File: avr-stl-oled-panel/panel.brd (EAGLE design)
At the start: 68 x 42.8 mm, 13 parts

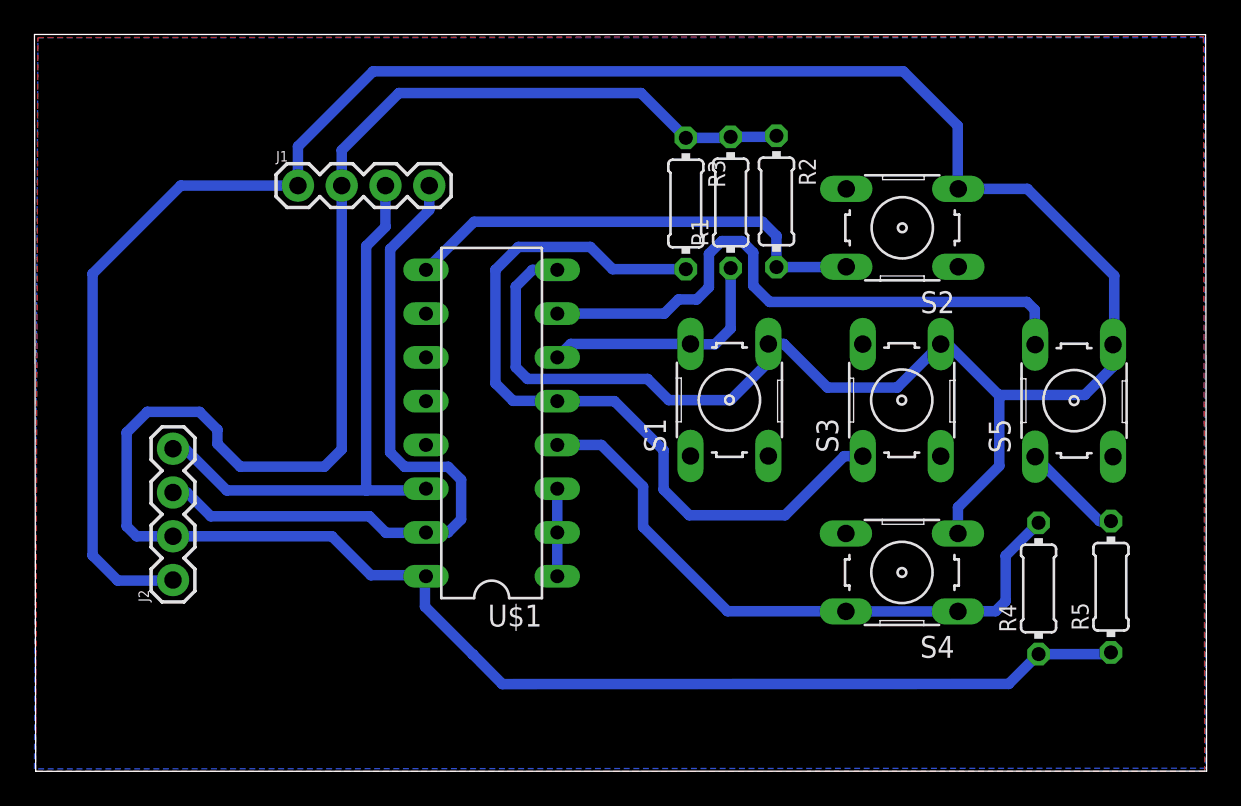
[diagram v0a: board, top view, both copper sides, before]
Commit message: adjusting oled position
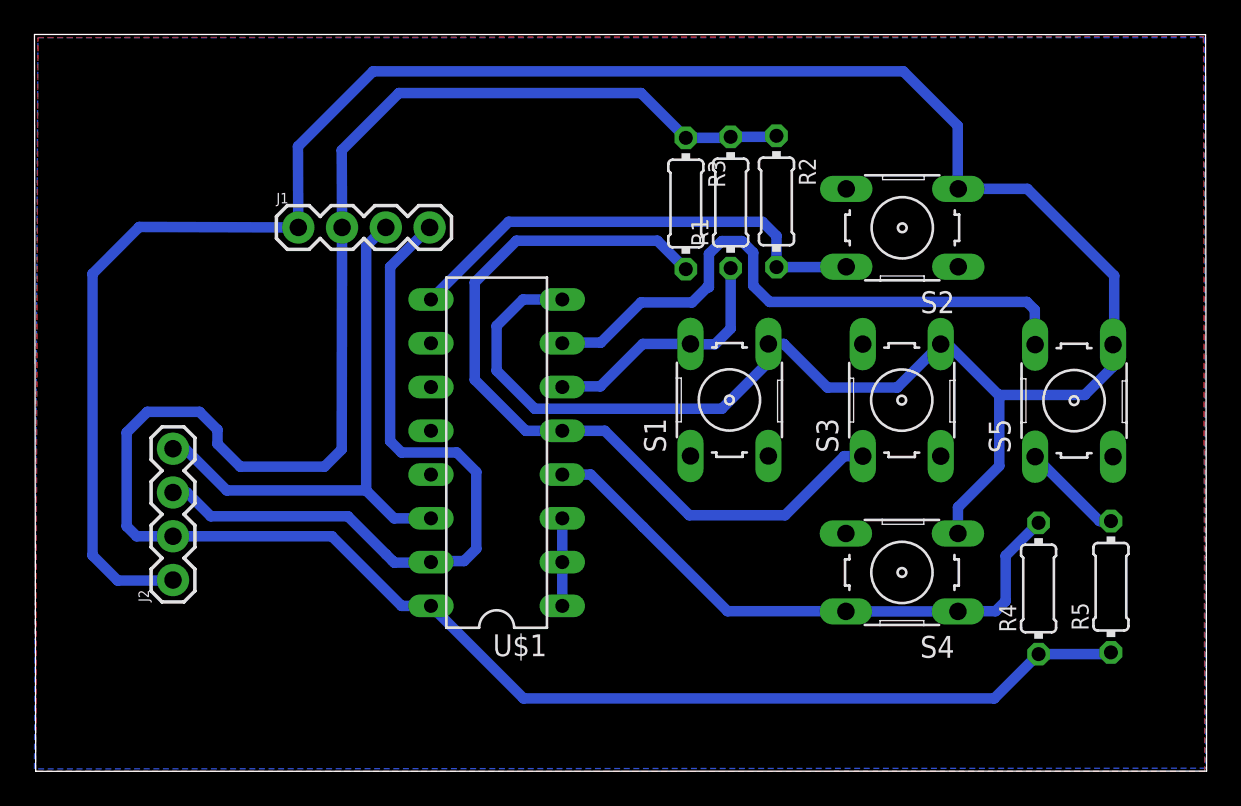
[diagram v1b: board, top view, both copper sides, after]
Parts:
- moved J1 2.43 mm to (15.3, 39.6)
- moved U$1 1.74 mm to (26.8, 26.5)
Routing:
- net GND: track 162.5 -> 164.9 mm
- net B3: track 37.0 -> 34.6 mm
- net N$4: track 41.5 -> 43.2 mm
- net N$5: track 33.9 -> 32.5 mm
- net B2: track 46.0 -> 46.8 mm

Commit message: changing oled panel chip to smd
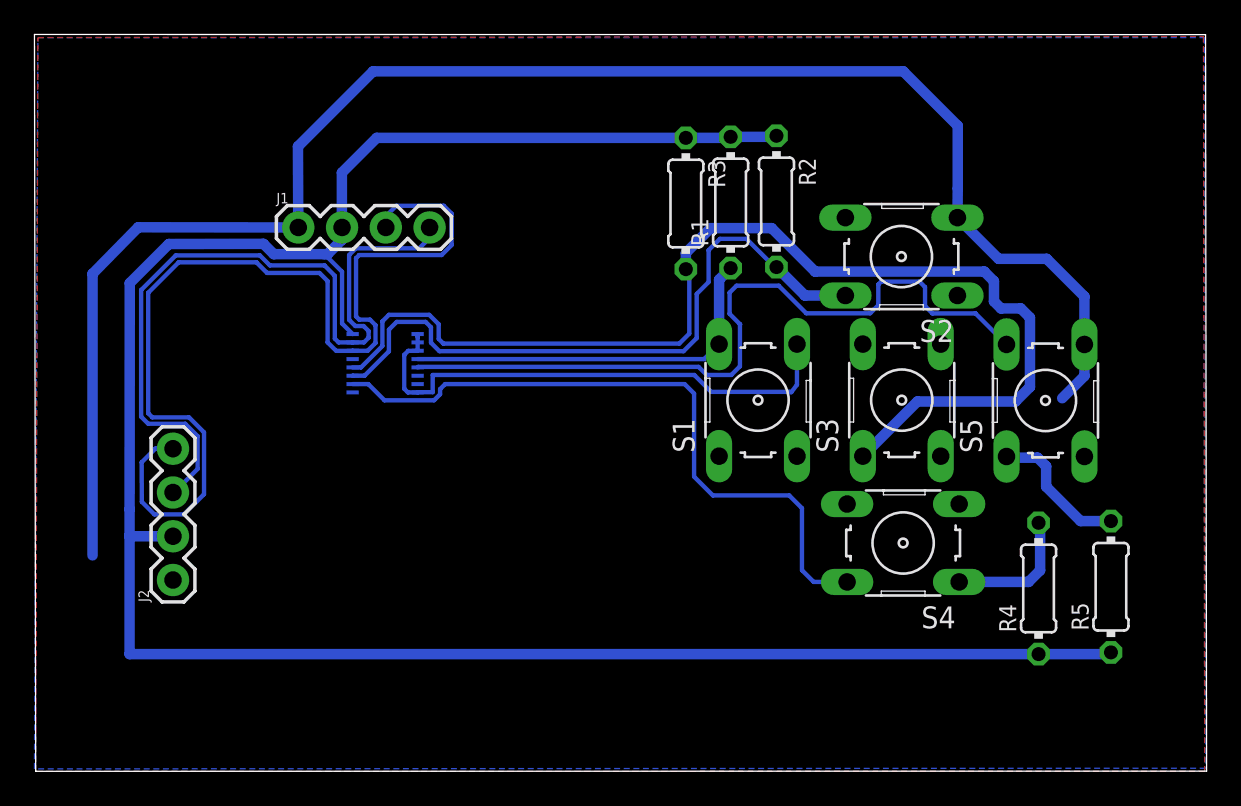
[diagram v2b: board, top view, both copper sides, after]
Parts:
- U$1: value PCF8574P -> PCF8574; device pcf8574p:DIL16 -> pcf8574p:SO16(SW)
- moved U$1 8.29 mm to (20.4, 31.7), flipped to the bottom, turned to 0 degrees
- moved S4 1.71 mm to (50.4, 21.3)
- moved S2 1.67 mm to (50.3, 37.9)
- moved S1 1.66 mm to (42.0, 29.6)
- moved S5 1.66 mm to (58.7, 29.6)
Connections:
- new net N$2: R4.2, S4.1
- net B0: now also U$1.4; no longer U$1.6
- net B1: now also U$1.11; no longer U$1.9
- net B2: now also U$1.12; no longer U$1.5
- net B3: now also U$1.10; no longer R4.2, S4.1, U$1.4
- net B4: now also U$1.5; no longer U$1.7
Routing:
- net GND: track 164.9 -> 127.4 mm
- net N$5: track 32.5 -> 59.8 mm
- net B2: track 46.8 -> 66.6 mm
- net B1: track 28.1 -> 38.5 mm
- net B4: track 35.8 -> 44.2 mm
- net B0: track 14.7 -> 22.5 mm
- net N$2: track 0.00 -> 7.77 mm
- net B3: track 34.6 -> 39.3 mm
- net N$1: track 5.95 -> 8.30 mm
- net VCC: track 128.1 -> 130.2 mm
- net N$4: track 43.2 -> 44.6 mm
